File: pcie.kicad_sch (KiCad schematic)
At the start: 28 parts, among them J10 OCuLink_x4_Amphenol_G14A42121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, J11 OCuLink_x4_Amphenol_G14A42121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

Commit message: [#93514] Propagate title and date across all of the sheets
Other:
- title: (none) -> Datacenter Secure Control Module Breakout Board
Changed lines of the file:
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@@
 	(generator_version "9.0")
 	(paper "A3")
+	(title_block
+		(title "Datacenter Secure Control Module Breakout Board")
+		(date "2021-12-16")
+		(rev "2.0.0")
+	)
 	(text "OCuLink HPMROOT\n"
 		(exclude_from_sim no)

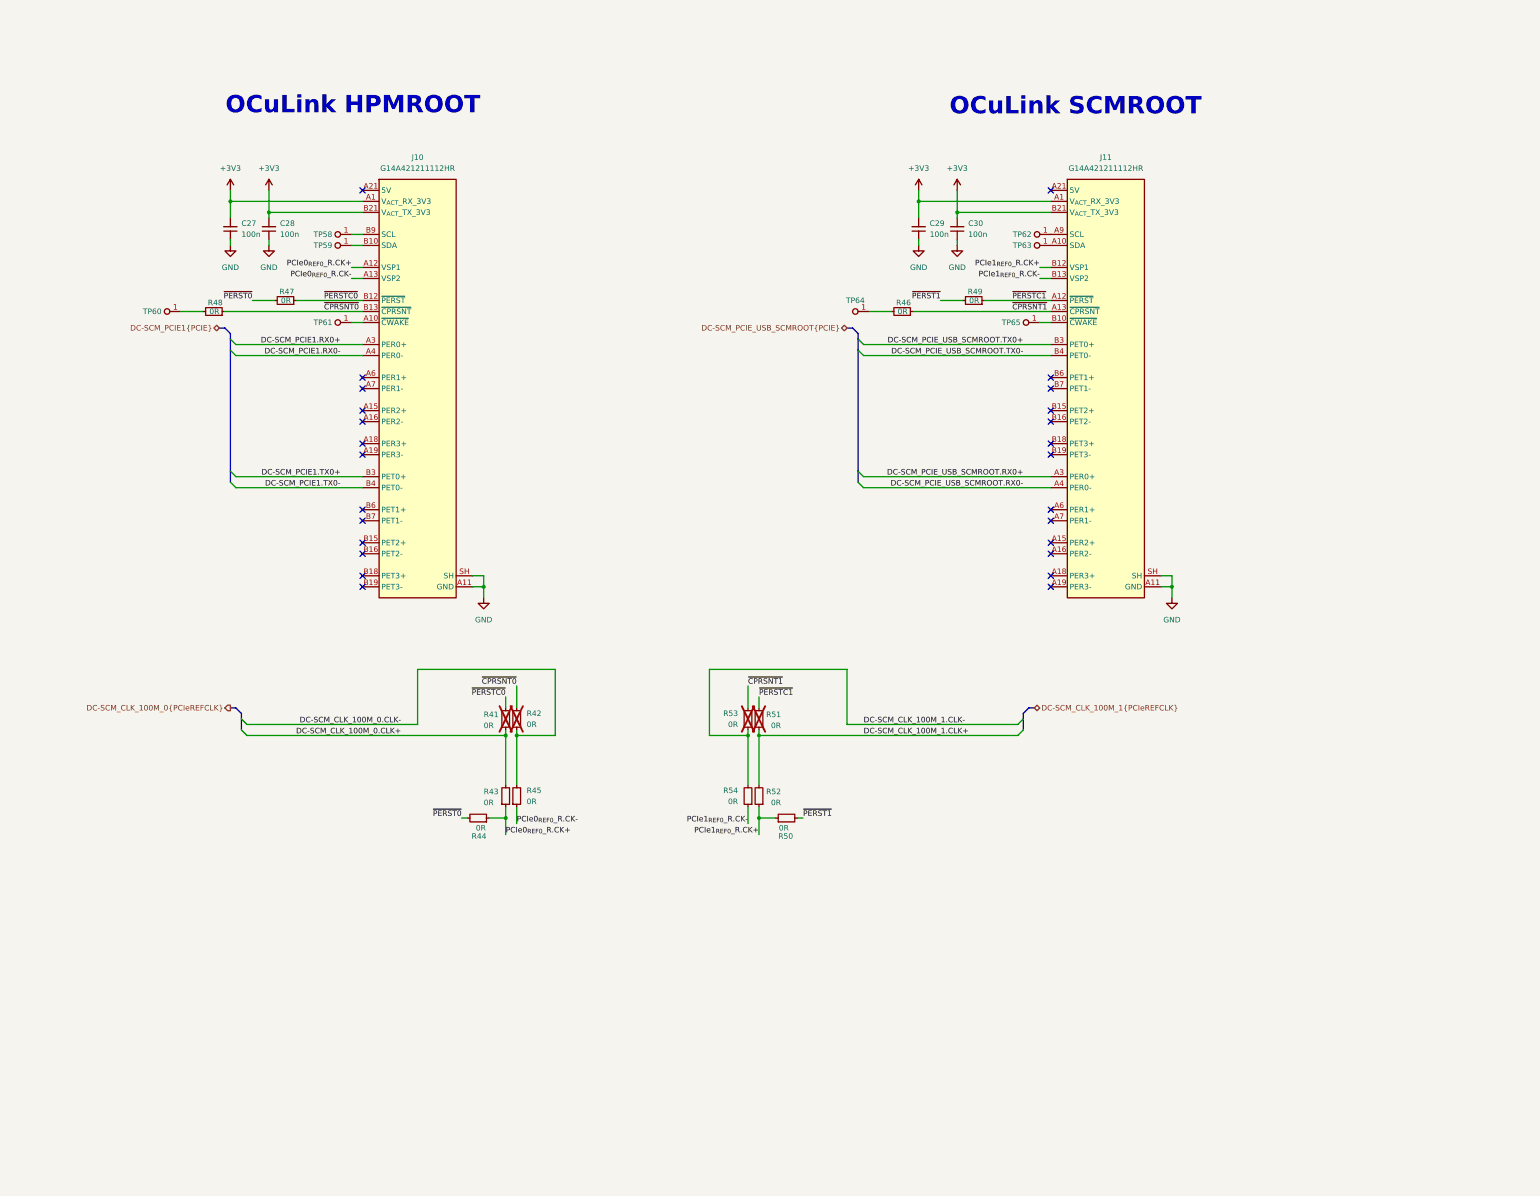
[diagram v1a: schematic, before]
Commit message: [#93514] Add separating lines, clean schematics
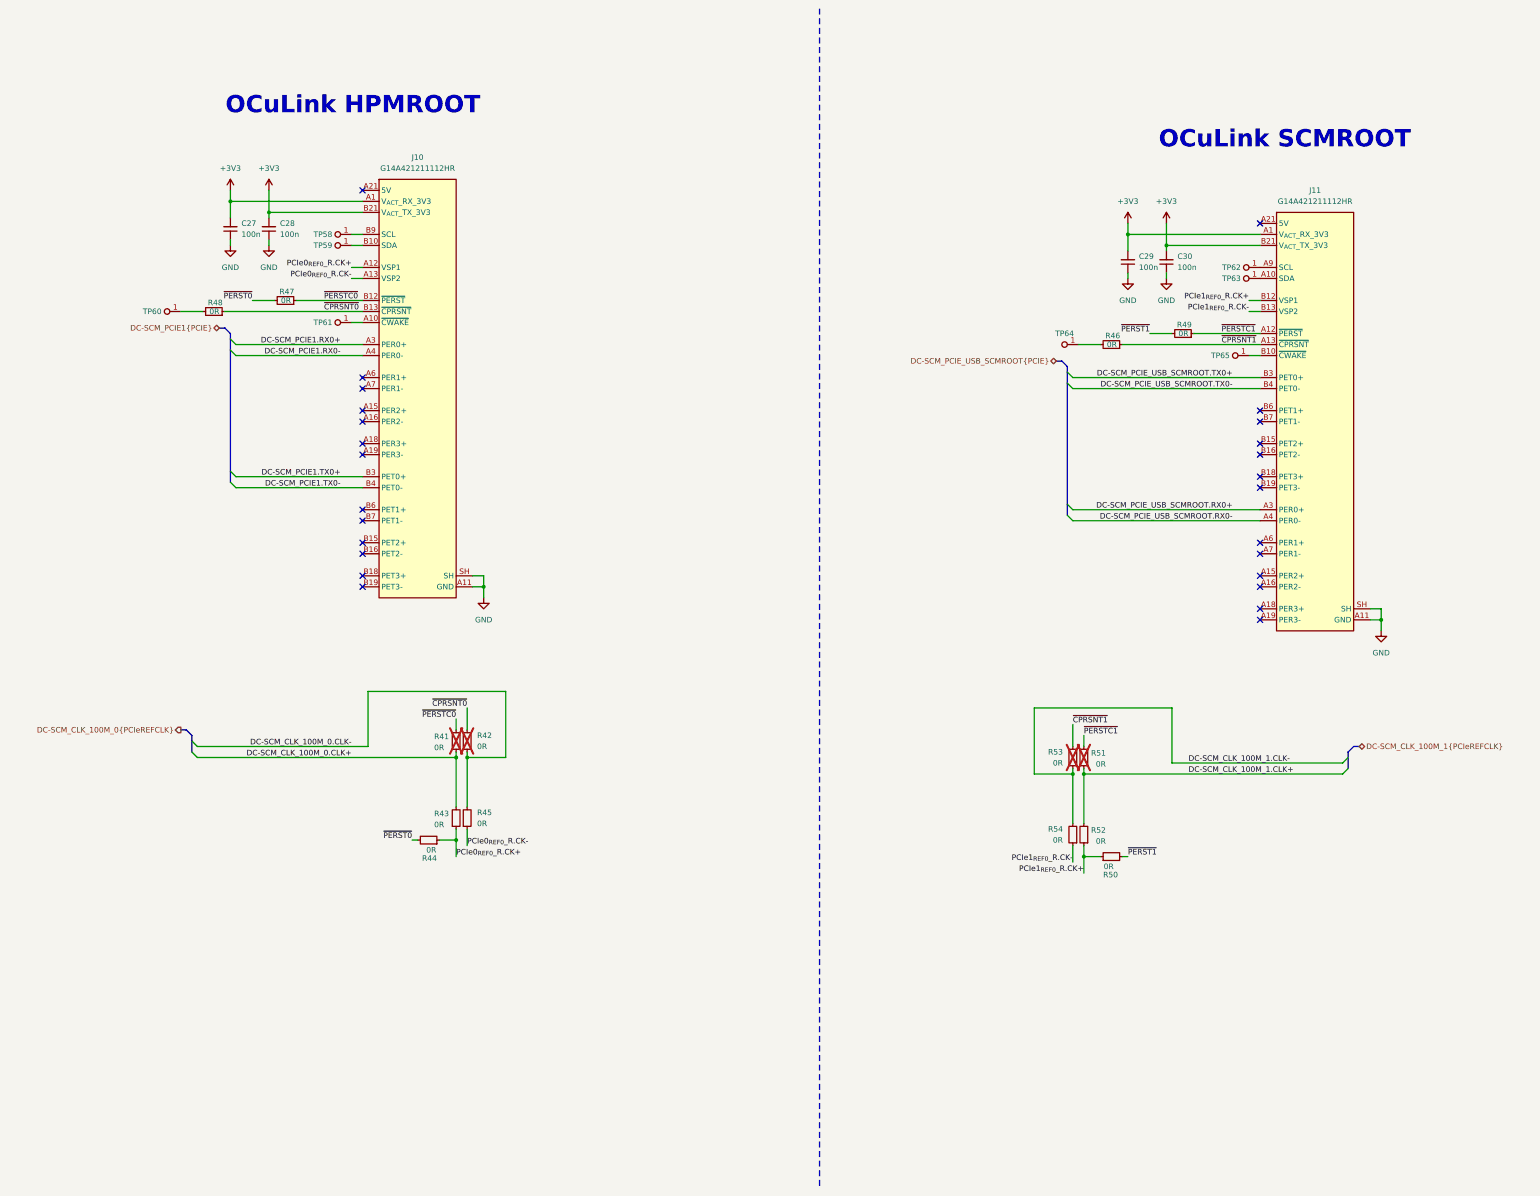
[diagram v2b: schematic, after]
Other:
- moved on the sheet: C29, C30, J11, R41, R42, R43, R44, R45, R46, R49, R50, R51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

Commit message: [#93514] Add PCIE SGMII header
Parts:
- added J17: PinHeader_2x10_P1.27mm_SMD_Shrouded, antmicro-footprints:PinHeader_2x10_P1.27mm_SMD_Shrouded, symbol antmicroGenericPinHeaders:PinHeader_2x10_P1.27mm_SMD_Shrouded
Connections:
- net GND: now also J17.10, J17.19, J17.20, J17.9
- new net DC-SCM_PCIE0_SGMII.RX0+: J17.5
- new net DC-SCM_PCIE0_SGMII.RX0-: J17.7
- new net DC-SCM_PCIE0_SGMII.RX1+: J17.15
- new net DC-SCM_PCIE0_SGMII.RX1-: J17.17
- new net DC-SCM_PCIE0_SGMII.RX2+: J17.6
- new net DC-SCM_PCIE0_SGMII.RX2-: J17.8
- new net DC-SCM_PCIE0_SGMII.RX3+: J17.16
- new net DC-SCM_PCIE0_SGMII.RX3-: J17.18
- new net DC-SCM_PCIE0_SGMII.TX0+: J17.1
- new net DC-SCM_PCIE0_SGMII.TX0-: J17.3
- new net DC-SCM_PCIE0_SGMII.TX1+: J17.11
- new net DC-SCM_PCIE0_SGMII.TX1-: J17.13
- new net DC-SCM_PCIE0_SGMII.TX2+: J17.2
- new net DC-SCM_PCIE0_SGMII.TX2-: J17.4
- new net DC-SCM_PCIE0_SGMII.TX3+: J17.12
- new net DC-SCM_PCIE0_SGMII.TX3-: J17.14
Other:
- moved on the sheet: C27, C28, C29, C30, J10, J11, R41, R42, R43, R44, R45, R46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

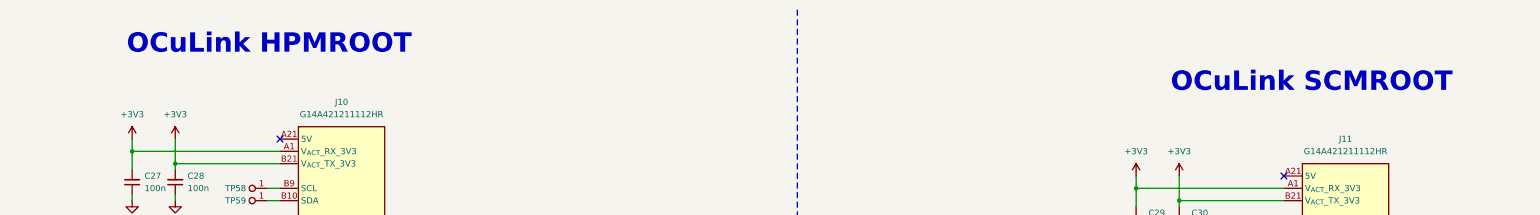
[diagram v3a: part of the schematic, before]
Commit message: [#93514] Align items to grid, add NC-SI testpads
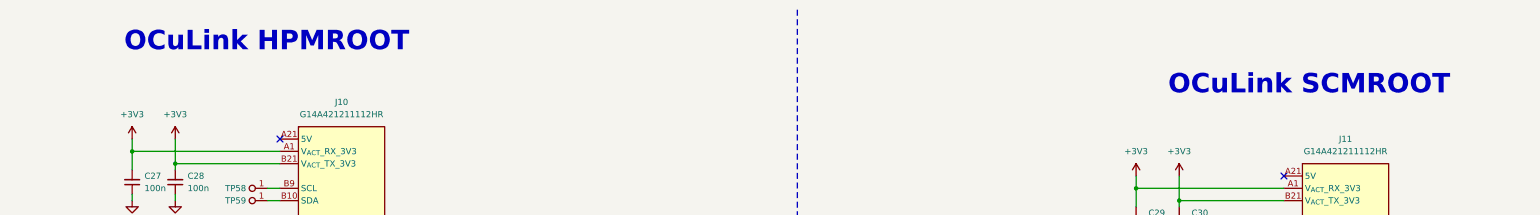
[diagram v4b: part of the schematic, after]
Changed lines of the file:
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@@
 	(text "OCuLink HPMROOT\n"
 		(exclude_from_sim no)
-		(at 130.048 22.098 0)
+		(at 129.54 21.59 0)
 		(effects
 			(font
@@
 	(text "OCuLink SCMROOT\n"
 		(exclude_from_sim no)
-		(at 344.678 29.972 0)
+		(at 344.17 30.48 0)
 		(effects
 			(font

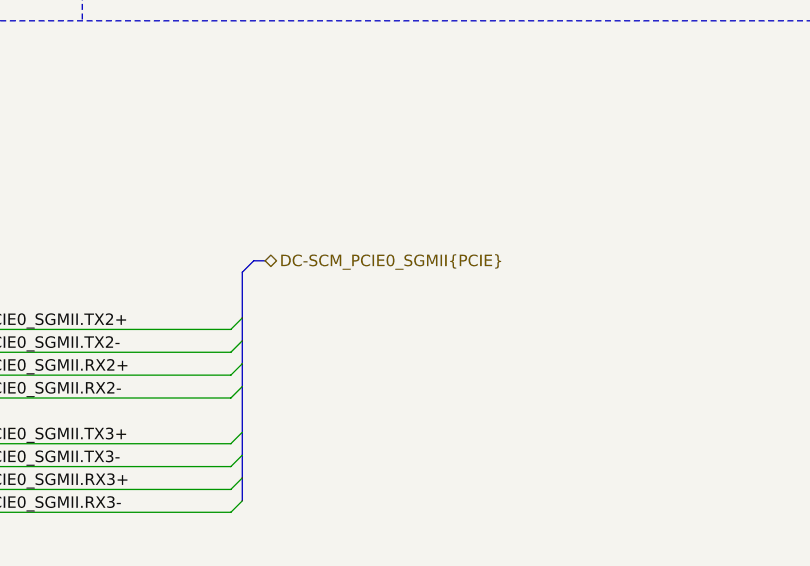
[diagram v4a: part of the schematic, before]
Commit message: [#93514] Reconnect SGMII connecotr
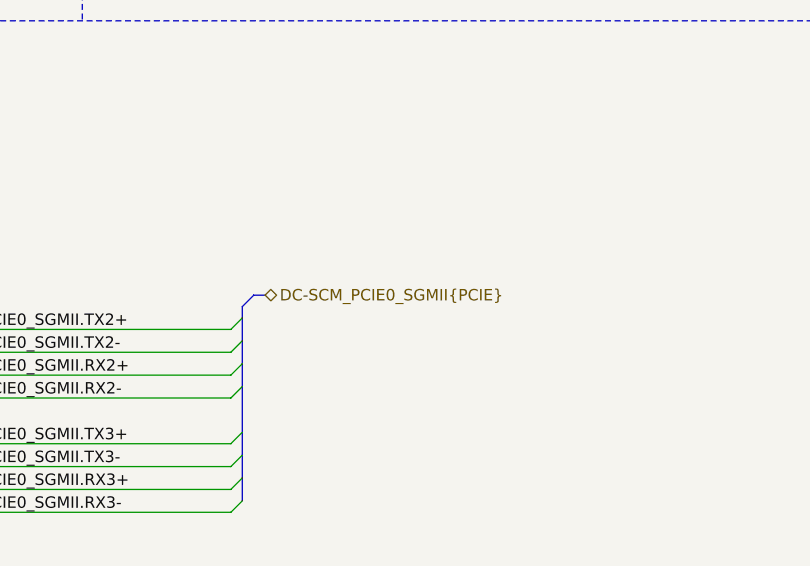
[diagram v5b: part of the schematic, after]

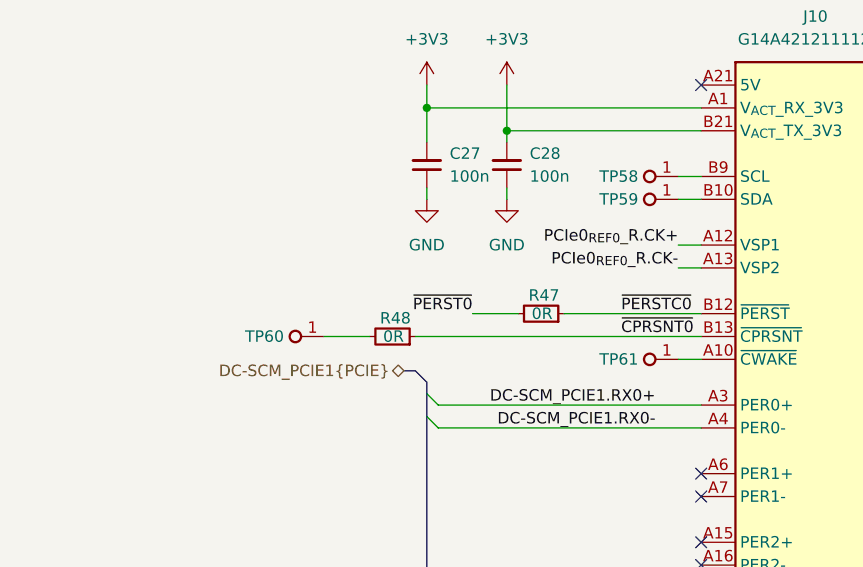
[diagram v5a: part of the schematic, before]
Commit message: [#93514] Add PERST to PCIE1
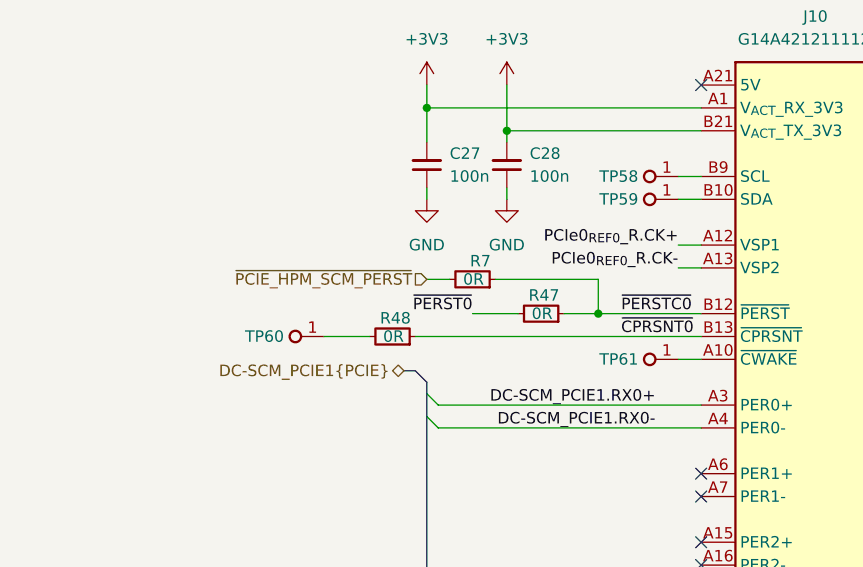
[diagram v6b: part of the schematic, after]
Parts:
- added R7: R_0R_0402, antmicro-footprints:R_0402_1005Metric, symbol antmicroResistors0402:R_0R_0402
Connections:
- net ~{PERSTC0}: now also R7.1
- new net ~{PCIE_HPM_SCM_PERST}: R7.2
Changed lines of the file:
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@@
 	)
 	(junction
+		(at 91.44 64.77)
+		(diameter 0)
+		(color 0 0 0 0)
+	)
+	(junction
 		(at 124.46 170.18)
 		(diameter 0)
@@
 	(wire
 		(pts
+			(xy 72.39 60.96) (xy 74.93 60.96)
+		)
+		(stroke
+			(width 0)
+			(type default)
+		)
+	)
+	(wire
+		(pts
 			(xy 182.88 245.11) (xy 226.06 245.11)
 		)
@@
 	(wire
 		(pts
+			(xy 91.44 64.77) (xy 87.63 64.77)
+		)
+		(stroke
+			(width 0)
+			(type default)
+		)
+	)
+	(wire
+		(pts
 			(xy 114.3 189.23) (xy 115.57 189.23)
 		)
@@
 		)
 	)
+	(wire
+		(pts
+			(xy 80.01 60.96) (xy 91.44 60.96)
+		)
+		(stroke
+			(width 0)
+			(type default)
+		)
+	)
 	(bus
 		(pts
@@
 		)
 	)
+	(wire
+		(pts
+			(xy 91.44 60.96) (xy 91.44 64.77)
+		)
+		(stroke
+			(width 0)
+			(type default)
+		)
+	)
 	(bus
 		(pts
@@
 	(wire
 		(pts
-			(xy 102.87 64.77) (xy 87.63 64.77)
+			(xy 102.87 64.77) (xy 91.44 64.77)
 		)
 		(stroke
@@
 		)
 	)
+	(hierarchical_label "~{PCIE_HPM_SCM_PERST}"
+		(shape input)
+		(at 72.39 60.96 180)
+		(effects
+			(font
+				(size 1.27 1.27)
+			)
+			(justify right)
+		)
+	)
 	(hierarchical_label "DC-SCM_CLK_100M_0{PCIeREFCLK}"
 		(shape output)
@@
 					(unit 1)
 				)
+			)
+		)
+	)
+	(symbol
+		(lib_name "R_0R_0402_1")
+		(lib_id "antmicroResistors0402:R_0R_0402")
+		(at 80.01 60.96 180)
+		(unit 1)
+		(exclude_from_sim no)
+		(in_bom yes)
+		(on_board yes)
+		(dnp no)
+		(property "Reference" "R7"
+			(at 79.502 58.928 0)
+			(effects
+				(font
+					(size 1.27 1.27)
+					(thickness 0.15)
+				)
+				(justify left)
+			)
+		)
+		(property "Value" "R_0R_0402"
+			(at 59.69 48.26 0)
+			(effects
+				(font
+					(size 1.27 1.27)
+					(thickness 0.15)
+				)
+				(justify left bottom)
+				(hide yes)
+			)
+		)
+		(property "Footprint" "antmicro-footprints:R_0402_1005Metric"
+			(at 59.69 45.72 0)
+			(effects
+				(font
+					(size 1.27 1.27)
+					(thickness 0.15)
+				)
+				(justify left bottom)
+				(hide yes)
+			)
+		)
+		(property "Datasheet" "https://industrial.panasonic.com/cdbs/www-data/pdf/RDA0000/AOA0000C301.pdf"
+			(at 59.69 43.18 0)
+			(effects
+				(font
+					(size 1.27 1.27)
+					(thickness 0.15)
+				)
+				(justify left bottom)
+				(hide yes)
+			)
+		)
+		(property "Description" "SMD Chip Resistor, Jumper, 0 ohm, 100 mW, 0402 [1005 Metric], Thick Film, General Purpose"
+			(at 59.69 27.94 0)
+			(effects
+				(font
+					(size 1.27 1.27)
+				)
+				(justify left bottom)
+				(hide yes)
+			)
+		)
+		(property "MPN" "ERJ2GE0R00X"
+			(at 59.69 40.64 0)
+			(effects
+				(font
+					(size 1.27 1.27)
+					(thickness 0.15)
+				)
+				(justify left bottom)
+				(hide yes)
+			)
+		)
+		(property "Manufacturer" "Panasonic"
+			(at 59.69 38.1 0)
+			(effects
+				(font
+					(size 1.27 1.27)
+					(thickness 0.15)
+				)
+				(justify left bottom)
+				(hide yes)
+			)
+		)
+		(property "License" "Apache-2.0"
+			(at 59.69 35.56 0)
+			(effects
+				(font
+					(size 1.27 1.27)
+					(thickness 0.15)
+				)
+				(justify left bottom)
+				(hide yes)
+			)
+		)
+		(property "Author" "Antmicro"
+			(at 59.69 33.02 0)
+			(effects
+				(font
+					(size 1.27 1.27)
+					(thickness 0.15)
+				)
+				(justify left bottom)
+				(hide yes)
+			)
+		)
+		(property "Val" "0R"
+			(at 78.74 60.96 0)
+			(effects
+				(font
+					(size 1.27 1.27)
+					(thickness 0.15)
+				)
+				(justify left)
+			)
+		)
+		(property "Tolerance" "~"
+			(at 59.69 50.8 0)
+			(effects
+				(font
+					(size 1.27 1.27)
+				)
+				(justify left bottom)
+				(hide yes)
+			)
+		)
+		(property "Current" "1A"
+			(at 59.69 30.48 0)
+			(effects
+				(font
+					(size 1.27 1.27)
+					(thickness 0.15)
+				)
+				(justify left bottom)
+				(hide yes)
+			)
+		)
+		(pin "2"
+		)
+		(pin "1"
+		)
+		(instances
+			(project "bmc-breakout-board"
+				(path "/5d67ef28-5805-4f87-b722-2926dabf7f6e/92b60d6e-26d5-4bc0-84f3-a50a27571d9f"
+					(reference "R7")
+					(unit 1)
+				)
